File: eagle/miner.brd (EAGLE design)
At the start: 83.8 x 63.5 mm, 30 parts, among them IC1 A3255-Q48

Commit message: miner with PIC
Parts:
- removed CONFIG_NI, CONFIG_PI, REPORT_N, REPORT_P, RSTN, XCLKIN: LSP10, solpad:LSP10
- added AVALON1: A3255-Q48, avalon:QFN48
- added C14: 22p, rcl:C0805
- added C15, C16, C17, C18, C19: 100n, rcl:C0805
- added IC2: 74LS14, 74xx-eu:SO14
- added IC3: 74LVC1G14SE-7, 74xx-little-de:SC70-5
- added IC4, U$1: TCN75, miner:SOIC8
- added JP1: PICkit 3, pinhead:1X06
- added Q1: SI501, miner:DFN4
- added R10, R11, R12, R13, R14, R15, R16, R17, R19, R20, R6, R7, R8, R9: 33, rcl:R0805
- added R18: 3k3, rcl:R0805
- added R5: 1k, rcl:R0805
- added U1RX, U1TX: LSP10, solpad:LSP10
- IC1: value A3255-Q48 -> PIC32MX220F032B; device avalon:QFN48 -> miner:SSOP28
- R4: value 33 -> 3k3
- moved R4 247.3 mm to (-22.9, -210.8)
- moved IC1 92.4 mm to (7.62, -58.4), turned to 0 degrees
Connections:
- new net CLK1: AVALON1.9, R8.1
- new net CLK10: R17.1
- new net CLK2: R9.1
- new net CLK3: R10.1
- new net CLK4: R11.1
- new net CLK5: R12.1
- new net CLK6: R13.1
- new net CLK7: R14.1
- new net CLK8: R15.1
- new net CLK9: R16.1
- new net N$11: Q1.3, R6.2, R7.2
- new net N$12: IC2.13, R7.1
- new net N$13: IC2.2, R5.1
- new net N$14: C14.1, IC2.3, R5.2
- new net N$15: IC2.11, IC2.12, IC2.9
- new net N$16: IC2.10, R10.2, R11.2, R12.2, R8.2, R9.2
- new net N$17: IC2.8, R13.2, R14.2, R15.2, R16.2, R17.2
- new net N$18: IC1.9, R6.1
- new net N$19: IC1.1, JP1.1
- new net N$20: R19.1, U1TX.MP
- new net N$21: IC1.2, JP1.4
- new net N$22: IC1.3, JP1.5
- new net N$23: R20.1, U1RX.MP
- new net OR: IC2.1, IC3.4
- new net OR_DELAY: IC1.26, IC2.4
- new net REPORT_N: AVALON1.16, AVALON1.17, IC2.5, IC3.1, R2.1, R3.1
- new net REPORT_N_I: IC1.6, IC2.6
- new net REPORT_P: IC3.2
- net +3V3: now also AVALON1.24, AVALON1.37, C15.1, C16.1, C17.1, C18.1, C19.1, IC1.13, IC1.28, IC2.14, IC3.5, IC4.8, JP1.2, Q1.4, R18.1, R4.1; no longer IC1.24, IC1.37
- net GND: now also AVALON1.12, AVALON1.23, AVALON1.27, AVALON1.38, AVALON1.5, AVALON1.8, AVALON1.EP-PAD, C14.2, C15.2, C16.2, C17.2, C18.2, C19.2, IC1.19, IC2.7, IC3.3, IC4.4, IC4.5, IC4.6, IC4.7, JP1.3, Q1.2; no longer IC1.12, IC1.23, IC1.38, IC1.5, IC1.EP-PAD
- net N$1: now also AVALON1.44, IC1.10; no longer IC1.44, RSTN.MP
- net N$10: now also AVALON1.43; no longer IC1.43
- net N$2: now also IC1.18, IC4.1, R4.2; no longer IC1.16, R2.1, REPORT_N.MP
- net N$3: now also IC4.2, R18.2; no longer R3.1, REPORT_P.MP
- net N$4: now also IC1.11, R19.2; no longer IC1.9, R4.2
- net N$5: now also IC1.24, R20.2; no longer R4.1, XCLKIN.MP
- net N$6: now also AVALON1.1, IC1.12; no longer CONFIG_PI.MP, IC1.1
- net N$7: now also AVALON1.2, IC1.4; no longer CONFIG_NI.MP, IC1.2
- net N$8: now also AVALON1.36; no longer IC1.36
- net N$9: now also AVALON1.35; no longer IC1.35
- net VDD: now also AVALON1.10, AVALON1.11, AVALON1.13, AVALON1.14, AVALON1.15, AVALON1.18, AVALON1.19, AVALON1.20, AVALON1.21, AVALON1.22, AVALON1.25, AVALON1.26, AVALON1.28, AVALON1.29, AVALON1.3, AVALON1.30, AVALON1.31, AVALON1.32, AVALON1.33, AVALON1.34, AVALON1.39, AVALON1.4, AVALON1.40, AVALON1.41, AVALON1.42, AVALON1.45, AVALON1.46, AVALON1.47, AVALON1.48, AVALON1.6, AVALON1.7; no longer IC1.10, IC1.11, IC1.13, IC1.14, IC1.15, IC1.18, IC1.19, IC1.20, IC1.21, IC1.22, IC1.25, IC1.26, IC1.28, IC1.29, IC1.3, IC1.30, IC1.31, IC1.32, IC1.33, IC1.34, IC1.39, IC1.4, IC1.40, IC1.41, IC1.42, IC1.45, IC1.46, IC1.47, IC1.48, IC1.6, IC1.7

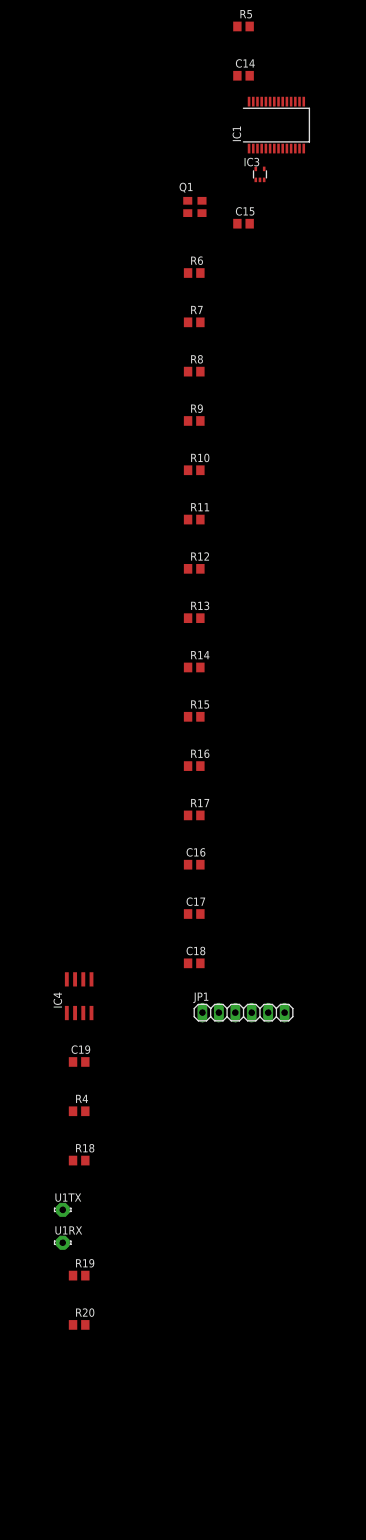
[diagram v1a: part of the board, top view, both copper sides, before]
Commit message: FPGA implementation converted to PIC firmware
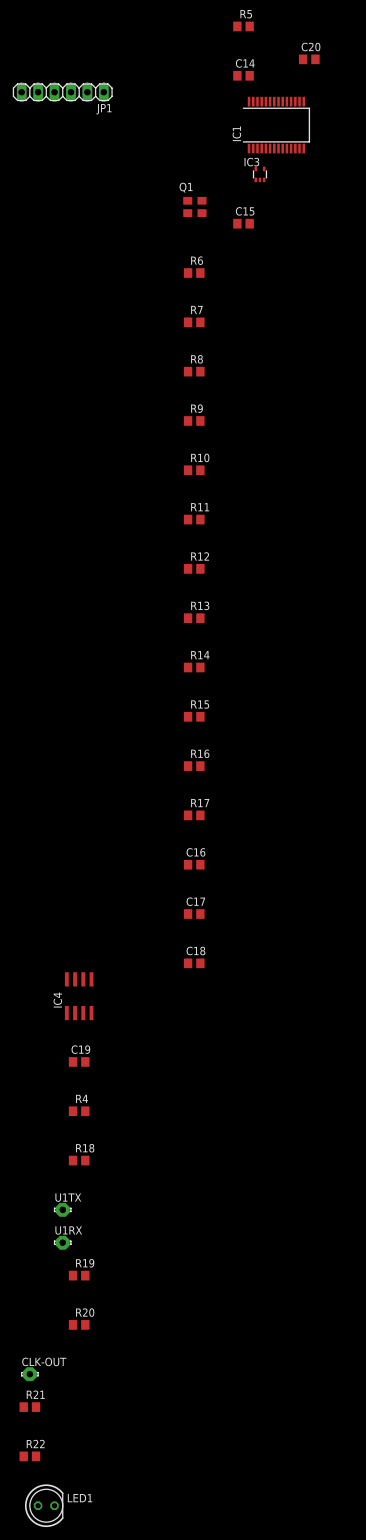
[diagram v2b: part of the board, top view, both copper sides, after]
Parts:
- added C20: 10u, rcl:C0805
- added CLK-OUT: LSP10, solpad:LSP10
- added LED1: (no value), led:LED5MM
- added R21: 10k, rcl:R0805
- added R22: 1k, rcl:R0805
- IC2: value 74LS14 -> 74LCX14
- moved JP1 145.0 mm to (-25.4, -53.3), turned to 180 degrees
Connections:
- net N$19 renamed VPP
- net N$21 renamed PGD
- net N$22 renamed PGC
- new net N$19: C20.1, IC1.20
- new net N$21: CLK-OUT.MP, IC1.10
- new net N$22: IC1.11, R22.1
- new net N$24: LED1.A, R22.2
- net +3V3: now also R21.2; no longer JP1.2
- net GND: now also C20.2, LED1.K
- net N$1: now also IC1.5; no longer IC1.10
- net N$20: now also R21.1
- net N$4: now also IC1.7; no longer IC1.11
- net REPORT_N: no longer AVALON1.17, R3.1
- net REPORT_P: now also AVALON1.17, R3.1
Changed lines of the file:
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@@
 <element name="C12" library="rcl" package="C0805" value="0.47u" x="66.04" y="20.32"/>
 <element name="C13" library="rcl" package="C0805" value="0.47u" x="58.42" y="12.7" rot="R270"/>
-<element name="IC2" library="74xx-eu" package="SO14" value="74LS14" x="7.62" y="-5.08"/>
+<element name="IC2" library="74xx-eu" package="SO14" value="74LCX14" x="7.62" y="-5.08"/>
 <element name="R5" library="rcl" package="R0805" value="1k" x="2.54" y="-43.18"/>
 <element name="C14" library="rcl" package="C0805" value="22p" x="2.54" y="-50.8"/>
@@
 <element name="C17" library="rcl" package="C0805" value="100n" x="-5.08" y="-180.34"/>
 <element name="C18" library="rcl" package="C0805" value="100n" x="-5.08" y="-187.96"/>
-<element name="JP1" library="pinhead" package="1X06" value="PICkit 3" x="2.54" y="-195.58"/>
+<element name="JP1" library="pinhead" package="1X06" value="PICkit 3" x="-25.4" y="-53.34" rot="R180"/>
 <element name="U$1" library="miner" package="SOIC8" value="TCN75" x="-12.383" y="0"/>
 <element name="IC4" library="miner" package="SOIC8" value="TCN75" x="-22.86" y="-193.04"/>
@@
 <element name="R19" library="rcl" package="R0805" value="33" x="-22.86" y="-236.22"/>
 <element name="R20" library="rcl" package="R0805" value="33" x="-22.86" y="-243.84"/>
+<element name="C20" library="rcl" package="C0805" value="10u" x="12.7" y="-48.26"/>
+<element name="CLK-OUT" library="solpad" package="LSP10" value="LSP10" x="-30.48" y="-251.46"/>
+<element name="R21" library="rcl" package="R0805" value="10k" x="-30.48" y="-256.54"/>
+<element name="R22" library="rcl" package="R0805" value="1k" x="-30.48" y="-264.16"/>
+<element name="LED1" library="led" package="LED5MM" value="" x="-27.94" y="-271.78"/>
 </elements>
 <signals>
@@
 <contactref element="IC4" pad="6"/>
 <contactref element="IC4" pad="5"/>
+<contactref element="C20" pad="2"/>
+<contactref element="LED1" pad="K"/>
 <wire x1="-20.955" y1="-195.64" x2="-21.91" y2="-203.2" width="0" layer="19" extent="1-1"/>
 <wire x1="-20.955" y1="-190.44" x2="-20.955" y2="-195.64" width="0" layer="19" extent="1-1"/>
@@
 <wire x1="-4.13" y1="-180.34" x2="-4.13" y2="-187.96" width="0" layer="19" extent="1-1"/>
 <wire x1="-4.13" y1="-172.72" x2="-4.13" y2="-180.34" width="0" layer="19" extent="1-1"/>
-<wire x1="1.27" y1="-195.58" x2="-4.13" y2="-187.96" width="0" layer="19" extent="1-1"/>
+<wire x1="-26.67" y1="-271.78" x2="-21.91" y2="-203.2" width="0" layer="19" extent="1-1"/>
 <wire x1="3.49" y1="-73.66" x2="-4.13" y2="-172.72" width="0" layer="19" extent="1-1"/>
 <wire x1="5.73" y1="-66.89" x2="3.49" y2="-73.66" width="0" layer="19" extent="1-1"/>
@@
 <wire x1="3.49" y1="-50.8" x2="4.045" y2="-54.795" width="0" layer="19" extent="1-1"/>
 <wire x1="-3.88" y1="-72.02" x2="3.49" y2="-73.66" width="0" layer="19" extent="1-1"/>
-<wire x1="11.43" y1="-8.1534" x2="3.49" y2="-50.8" width="0" layer="19" extent="1-1"/>
+<wire x1="13.65" y1="-48.26" x2="9.245" y2="-54.795" width="0" layer="19" extent="1-1"/>
+<wire x1="-24.13" y1="-53.34" x2="-3.88" y2="-72.02" width="0" layer="19" extent="1-1"/>
+<wire x1="11.43" y1="-8.1534" x2="13.65" y2="-48.26" width="0" layer="19" extent="1-1"/>
 <wire x1="40.64" y1="9.21" x2="11.43" y2="-8.1534" width="0" layer="19" extent="1-1"/>
 <wire x1="47.31" y1="20.32" x2="40.64" y2="9.21" width="0" layer="19" extent="1-1"/>
@@
 <contactref element="IC3" pad="5"/>
 <contactref element="C18" pad="1"/>
-<contactref element="JP1" pad="2"/>
 <contactref element="R4" pad="1"/>
 <contactref element="R18" pad="1"/>
 <contactref element="IC4" pad="8"/>
 <contactref element="C19" pad="1"/>
+<contactref element="R21" pad="2"/>
 <wire x1="-23.81" y1="-210.82" x2="-23.81" y2="-218.44" width="0" layer="19" extent="1-1"/>
 <wire x1="-23.81" y1="-203.2" x2="-23.81" y2="-210.82" width="0" layer="19" extent="1-1"/>
@@
 <wire x1="-6.03" y1="-180.34" x2="-6.03" y2="-187.96" width="0" layer="19" extent="1-1"/>
 <wire x1="-6.03" y1="-172.72" x2="-6.03" y2="-180.34" width="0" layer="19" extent="1-1"/>
-<wire x1="-1.27" y1="-195.58" x2="-6.03" y2="-187.96" width="0" layer="19" extent="1-1"/>
+<wire x1="-29.53" y1="-256.54" x2="-23.81" y2="-218.44" width="0" layer="19" extent="1-1"/>
 <wire x1="1.59" y1="-73.66" x2="-6.03" y2="-172.72" width="0" layer="19" extent="1-1"/>
 <wire x1="-6.08" y1="-70.12" x2="1.59" y2="-73.66" width="0" layer="19" extent="1-1"/>
@@
 <contactref element="AVALON1" pad="44"/>
 <contactref element="R1" pad="2"/>
-<contactref element="IC1" pad="10"/>
+<contactref element="IC1" pad="5"/>
 <wire x1="40.64" y1="11.11" x2="52.505" y2="20.07" width="0" layer="19" extent="1-1"/>
-<wire x1="9.245" y1="-62.045" x2="40.64" y2="11.11" width="0" layer="19" extent="1-1"/>
+<wire x1="5.995" y1="-62.045" x2="40.64" y2="11.11" width="0" layer="19" extent="1-1"/>
 </signal>
 <signal name="N$6">
@@
 <contactref element="R2" pad="1"/>
 <contactref element="AVALON1" pad="16"/>
-<contactref element="AVALON1" pad="17"/>
-<contactref element="R3" pad="1"/>
-<wire x1="60.255" y1="20.07" x2="60.255" y2="19.57" width="0" layer="19" extent="1-1"/>
 <wire x1="60.96" y1="8.57" x2="60.255" y2="19.57" width="0" layer="19" extent="1-1"/>
-<wire x1="66.04" y1="8.57" x2="60.96" y2="8.57" width="0" layer="19" extent="1-1"/>
 <wire x1="8.89" y1="-8.1534" x2="60.96" y2="8.57" width="0" layer="19" extent="1-1"/>
 <wire x1="4.43" y1="-66.89" x2="8.89" y2="-8.1534" width="0" layer="19" extent="1-1"/>
-</signal>
-<signal name="REPORT_P">
-<contactref element="IC3" pad="2"/>
 </signal>
 <signal name="OR">
@@
 <wire x1="8.595" y1="-62.045" x2="-6.03" y2="-81.28" width="0" layer="19" extent="1-1"/>
 </signal>
-<signal name="N$19">
+<signal name="VPP">
 <contactref element="IC1" pad="1"/>
 <contactref element="JP1" pad="1"/>
-<wire x1="3.395" y1="-62.045" x2="-3.81" y2="-195.58" width="0" layer="19" extent="1-1"/>
-</signal>
-<signal name="N$21">
+<wire x1="3.395" y1="-62.045" x2="-19.05" y2="-53.34" width="0" layer="19" extent="1-1"/>
+</signal>
+<signal name="PGD">
 <contactref element="JP1" pad="4"/>
 <contactref element="IC1" pad="2"/>
-<wire x1="4.045" y1="-62.045" x2="3.81" y2="-195.58" width="0" layer="19" extent="1-1"/>
-</signal>
-<signal name="N$22">
+<wire x1="4.045" y1="-62.045" x2="-26.67" y2="-53.34" width="0" layer="19" extent="1-1"/>
+</signal>
+<signal name="PGC">
 <contactref element="JP1" pad="5"/>
 <contactref element="IC1" pad="3"/>
-<wire x1="4.695" y1="-62.045" x2="6.35" y2="-195.58" width="0" layer="19" extent="1-1"/>
+<wire x1="4.695" y1="-62.045" x2="-29.21" y2="-53.34" width="0" layer="19" extent="1-1"/>
 </signal>
 <signal name="N$2">
@@
 <wire x1="10.545" y1="-54.795" x2="-23.495" y2="-195.64" width="0" layer="19" extent="1-1"/>
 </signal>
-<signal name="N$4">
-<contactref element="IC1" pad="11"/>
-<contactref element="R19" pad="2"/>
-<wire x1="-21.91" y1="-236.22" x2="9.895" y2="-62.045" width="0" layer="19" extent="1-1"/>
-</signal>
 <signal name="N$5">
 <contactref element="IC1" pad="24"/>
@@
 <contactref element="R19" pad="1"/>
 <contactref element="U1TX" pad="MP"/>
+<contactref element="R21" pad="1"/>
 <wire x1="-23.81" y1="-236.22" x2="-25.4" y2="-226.06" width="0" layer="19" extent="1-1"/>
+<wire x1="-31.43" y1="-256.54" x2="-23.81" y2="-236.22" width="0" layer="19" extent="1-1"/>
 </signal>
 <signal name="N$23">
@@
 <wire x1="-25.4" y1="-231.14" x2="-23.81" y2="-243.84" width="0" layer="19" extent="1-1"/>
 </signal>
+<signal name="REPORT_P">
+<contactref element="AVALON1" pad="17"/>
+<contactref element="R3" pad="1"/>
+<contactref element="IC3" pad="2"/>
+<wire x1="66.04" y1="8.57" x2="60.255" y2="20.07" width="0" layer="19" extent="1-1"/>
+<wire x1="5.08" y1="-66.89" x2="66.04" y2="8.57" width="0" layer="19" extent="1-1"/>
+</signal>
+<signal name="N$19">
+<contactref element="IC1" pad="20"/>
+<contactref element="C20" pad="1"/>
+<wire x1="11.75" y1="-48.26" x2="8.595" y2="-54.795" width="0" layer="19" extent="1-1"/>
+</signal>
+<signal name="N$21">
+<contactref element="IC1" pad="10"/>
+<contactref element="CLK-OUT" pad="MP"/>
+<wire x1="-30.48" y1="-251.46" x2="9.245" y2="-62.045" width="0" layer="19" extent="1-1"/>
+</signal>
+<signal name="N$4">
+<contactref element="IC1" pad="7"/>
+<contactref element="R19" pad="2"/>
+<wire x1="-21.91" y1="-236.22" x2="7.295" y2="-62.045" width="0" layer="19" extent="1-1"/>
+</signal>
+<signal name="N$22">
+<contactref element="IC1" pad="11"/>
+<contactref element="R22" pad="1"/>
+<wire x1="-31.43" y1="-264.16" x2="9.895" y2="-62.045" width="0" layer="19" extent="1-1"/>
+</signal>
+<signal name="N$24">
+<contactref element="R22" pad="2"/>
+<contactref element="LED1" pad="A"/>
+<wire x1="-29.53" y1="-264.16" x2="-29.21" y2="-271.78" width="0" layer="19" extent="1-1"/>
+</signal>
 </signals>
